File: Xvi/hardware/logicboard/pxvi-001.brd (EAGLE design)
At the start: 91 x 90 mm, 58 parts, among them J0 12V, J1 MKR, J7 DIN5, Q1 60V/32A/35mΩ, Q10 60V/32A/35mΩ, Q11 60V/32A/35mΩ, Q12 60V/32A/35mΩ, Q13 60V/32A/35mΩ, Q14 60V/32A/35mΩ, Q15 60V/32A/35mΩ, Q16 60V/32A/35mΩ, Q2 60V/32A/35mΩ, Q3 60V/32A/35mΩ, Q4 60V/32A/35mΩ, Q5 60V/32A/35mΩ, Q6 60V/32A/35mΩ, Q7 60V/32A/35mΩ, Q8 60V/32A/35mΩ, Q9 60V/32A/35mΩ, U1 DS18B20, X2 ADAFRUIT-PCA9685

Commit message: Guide for fan.
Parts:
- moved D13 2.00 mm to (51.5, 26.0)
- moved D16 2.00 mm to (84.5, 26.0)
- turned RN1 to 270 degrees
- turned RN2 to 270 degrees
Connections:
- net VCC: now also JP1.1
- net VIN: no longer JP1.1
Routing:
- net PWM06: track 216.4 -> 121.6 mm, vias 4 -> 3
- net GND: track 557.2 -> 468.9 mm, vias 1 -> 3
- net THS: track 197.7 -> 120.5 mm, vias 3 -> 4
- net VCC: track 210.6 -> 284.2 mm
- net PWM15: track 176.3 -> 132.5 mm
- net PWM04: track 134.9 -> 94.9 mm
- net SDA: track 163.1 -> 201.1 mm, vias 2 -> 5
- net PWM08: track 102.7 -> 139.0 mm, vias 3 -> 4
- net PWM10: track 161.6 -> 129.8 mm, vias 1 -> 5
- net PWM05: track 137.0 -> 107.9 mm, vias 3 -> 1
- net PWM03: track 129.7 -> 101.2 mm, vias 0 -> 3
- net LD07: track 87.8 -> 59.8 mm, vias 6 -> 0
- net LD10: track 75.0 -> 50.2 mm
- net VIN: track 399.4 -> 377.4 mm, vias 6 -> 2
- net PWM02: track 127.6 -> 106.5 mm
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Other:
- board text added: "DC5V"
- board text added: "Holes are design guide for 30mm fan"
- board text removed: "0"
- board text removed: "1"
- board text removed: "2"
- board text removed: "3"
- board text removed: "A"

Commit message: Xvi/LightDrive Port.
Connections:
- net GND: now also SV2.34
- net MNTR: now also SV2.33
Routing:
- net LD00: track 58.2 -> 185.1 mm, vias 3 -> 16
- net MNTR: track 0.00 -> 62.1 mm
- net PWM10: track 129.8 -> 173.8 mm, vias 5 -> 2
- net GND: track 468.9 -> 509.0 mm, vias 3 -> 5
- net PWM12: track 104.6 -> 137.9 mm, vias 5 -> 3
- net PWM01: track 97.2 -> 130.0 mm, vias 2 -> 3
- net PWM07: track 105.1 -> 137.9 mm, vias 6 -> 2
- net PWM15: track 132.5 -> 157.6 mm, vias 2 -> 1
- net PWM11: track 151.5 -> 175.0 mm
- net PWM04: track 94.9 -> 116.1 mm, vias 3 -> 1
- net PWM05: track 107.9 -> 128.8 mm, vias 1 -> 0
- net PWM00: track 109.8 -> 128.2 mm, vias 4 -> 3
- net VIN: track 377.4 -> 393.9 mm, vias 2 -> 4
- net LD01: track 77.7 -> 62.0 mm, vias 6 -> 3
- net PWM14: track 131.7 -> 146.3 mm, vias 4 -> 1
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- removed copper zone on layer 1, net GND
- removed copper zone on layer 16, net GND
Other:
- board text added: "LightDrive"
- board text added: "Pineapple Xvi 0.0.4-X"
- board text removed: "Pineapple Xvi 0.0.3-X"

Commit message: Redesign.
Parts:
- removed D0: (no value), SparkFun-DiscreteSemi:DIODE-1N4148
- removed D10, D11, D12, D13, D14, D15, D16, D2, D4, D5, D6, D7, D8, D9: 200mA/100V/1V, SparkFun-DiscreteSemi:DIODE-1N4148
- removed JG1: Grove/1, Connector:4P-2.0-90D
- removed JG2: Grove/2, Connector:4P-2.0-90D
- removed LD1: Red/Green, led:DUOLED-C-5MM
- removed R6: 220, resistor:0204/5
- removed RN1: 10k, resistor-net:RN-9
- removed SV2: LD, con-ml:ML34L
- removed SV3: Testport II, pinhead:2X07
- removed X2: ADAFRUIT-PCA9685, adafruit-pca9685:ADAFRUIT-PCA9685-FOOTPRINT
- added C1: 22u, rcl:C025-050X050
- added C10, C4: 100n, rcl:C025-024X044
- added C11: 100n, resistor:C025-024X044
- added C2: 470n, rcl:C050-024X044
- added C3: 1u, rcl:C050-024X044
- added C5: 10n, resistor:C025-024X044
- added DD1, DD10, DD11, DD12, DD13, DD14, DD15, DD16, DD2, DD3, DD4, DD5, DD6, DD7, DD8, DD9: 200mA/100V/1V, SparkFun-DiscreteSemi:DIODE-1N4148
- added F1: 1.8A, fuse:TE5
- added J2, J3: (no value), Connector:4P-2.0-90D
- added J20: (no value), SparkFun-Connectors:1X04_1.27MM
- added J5: SPI, SparkFun-Connectors:1X06_1.27MM
- added J6: LED, SparkFun-Connectors:JST-3-PTH-VERT
- added JP6: LED, pinhead:1X03
- added R1: 220, resistor:0204/5
- added R3: 1k, resistor:0204/5
- added SV1: (no value), con-ml:ML34L
- added V1: 5V, v-reg:78XXL
- added X1: ADAFRUIT-PCA9685, adafruit-pca9685:ADAFRUIT-PCA9685-FOOTPRINT
- D1, D3: value 200mA/100V/1V -> (none)
- J0: value 12V -> (none)
- JP1: value FAN -> PWRSEL; device pinhead:1X02 -> pinhead:2X03
- R4, R5: value 330 -> 1k
- RN2: value 10k -> 4.7k; device resistor-net:RN-9 -> resistor-net:RN-5
- moved J0 64.8 mm to (85.5, 64.0)
- moved C6 64.3 mm to (38.5, 5.00)
- moved RN2 63.5 mm to (30.0, 19.5), turned to 0 degrees
- moved D3 57.6 mm to (32.0, 14.0)
- moved J1 46.9 mm to (94.0, 23.0)
- moved C7 46.2 mm to (35.5, 58.5), turned to 0 degrees
- moved JP1 45.2 mm to (86.0, 56.5)
- moved R5 44.0 mm to (35.5, 61.5), turned to 0 degrees
- moved RN3 39.5 mm to (50.0, 24.5), turned to 0 degrees
- moved U$1 37.5 mm to (7.00, 37.5), turned to 90 degrees
- moved R4 35.7 mm to (25.5, 61.5), turned to 0 degrees
- moved LOGO1 35.5 mm to (50.0, 34.0), flipped to the top
- moved Q9 35.4 mm to (80.0, 50.0)
- moved OK1 32.0 mm to (27.0, 53.0)
- moved Q13 30.5 mm to (80.0, 30.0)
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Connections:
- removed net MIDIINSND: D0.C, OK1.1, R6.1
- new net MIN: OK1.7, RN2.2
- new net MISNDA: D3.C, OK1.1, R1.1
- new net N$10: X1.PWM02
- new net N$11: X1.PWM03
- new net N$12: X1.PWM04
- new net N$13: X1.PWM05
- new net N$14: X1.PWM06
- new net N$15: X1.PWM07
- new net N$16: X1.PWM08
- new net N$17: X1.PWM09
- new net N$18: X1.PWM10
- new net N$19: X1.PWM11
- new net N$20: X1.PWM12
- new net N$21: X1.PWM13
- new net N$22: X1.PWM14
- new net N$23: X1.PWM15
- new net N$8: X1.PWM00
- new net N$9: X1.PWM01
- new net NMO2RTN: RN2.5
- new net NMORTN: RN2.4
- new net NMTRTN: RN2.3
- new net V+: C1.1, C2.1, D1.C, DD1.C, DD10.C, DD11.C, DD12.C, DD13.C, DD14.C, DD15.C, DD16.C, DD2.C, DD3.C, DD4.C, DD5.C, DD6.C, DD7.C, DD8.C, DD9.C, J0.3, JP1.1, SV1.10, SV1.12, SV1.14, SV1.16, SV1.18, SV1.2, SV1.20, SV1.22, SV1.24, SV1.26, SV1.28, SV1.30, SV1.32, SV1.4, SV1.6, SV1.8, V1.IN
- new net VCC/2: JP1.5, R3.2
- new net VOUT: F1.2, JP1.4, JP1.6
- new net VOUTRAW: C3.1, C4.1, D1.A, F1.1, V1.OUT
- net AREF: now also C10.1, R3.1
- net D7GATE: no longer SV3.11
- net DTCT0: no longer SV3.8
- net DTCT1: no longer SV3.10
- net DTCT2: no longer SV3.12
- net DTCT3: no longer SV3.14
- net GND: now also C1.2, C10.2, C11.2, C2.2, C3.2, C4.2, C5.2, J2.4, J3.4, J5.6, J6.2, JP6.2, SV1.34, V1.GND, X1.LGND, X1.LOE, X1.RGND; no longer JG1.4, JG2.4, JP1.2, LD1.C, RN1.1, RN2.1, SV2.34, SV3.5, X2.GND00, X2.GND01, X2.GND02, X2.GND03, X2.GND04, X2.GND05, X2.GND06, X2.GND07, X2.GND08, X2.GND09, X2.GND10, X2.GND11, X2.GND12, X2.GND13, X2.GND14, X2.GND15, X2.LGND, X2.LOE, X2.RGND
- net GPIO0: now also J20.3; no longer SV3.2
- net GPIO1: now also J20.4; no longer SV3.4
- net LD00: now also DD1.A, SV1.1; no longer D1.A, SV2.1
- net LD01: now also DD2.A, SV1.3; no longer D2.A, SV2.3
- net LD02: now also DD3.A, SV1.5; no longer D3.A, SV2.5
- net LD03: now also DD4.A, SV1.7; no longer D4.A, SV2.7
- net LD04: now also DD5.A, SV1.9; no longer D5.A, SV2.9
- net LD05: now also DD6.A, SV1.11; no longer D6.A, SV2.11
- net LD06: now also DD7.A, SV1.13; no longer D7.A, SV2.13
- net LD07: now also DD8.A, SV1.15; no longer D8.A, SV2.15
- net LD08: now also DD9.A, SV1.17; no longer D9.A, SV2.17
- net LD09: now also DD10.A, SV1.19; no longer D10.A, SV2.19
- net LD10: now also DD11.A, SV1.21; no longer D11.A, SV2.21
- net LD11: now also DD12.A, SV1.23; no longer D12.A, SV2.23
- net LD12: now also DD13.A, SV1.25; no longer D13.A, SV2.25
- net LD13: now also DD14.A, SV1.27; no longer D14.A, SV2.27
- net LD14: now also DD15.A, SV1.29; no longer D15.A, SV2.29
- net LD15: now also DD16.A, SV1.31; no longer D16.A, SV2.31
- net LED0A: now also J6.3, JP6.3; no longer LD1.AR
- net LED1A: now also J6.1, JP6.1; no longer LD1.AX
- net MIRTN: now also D3.A; no longer D0.A
- net MISND: now also R1.2; no longer R6.2
- net MISO: now also J5.1
- net MNTR: now also RN3.5, SV1.33; no longer SV2.33
- net MOSI: now also J5.4
- net PWM00: no longer RN1.2, X2.PWM00
- net PWM01: no longer RN1.3, X2.PWM01
- net PWM02: no longer RN1.4, X2.PWM02
- net PWM03: no longer RN1.5, X2.PWM03
- net PWM04: no longer RN1.6, X2.PWM04
- net PWM05: no longer RN1.7, X2.PWM05
- net PWM06: no longer RN1.8, X2.PWM06
- net PWM07: no longer RN1.9, X2.PWM07
- net PWM08: no longer RN2.2, X2.PWM08
- net PWM09: no longer RN2.3, X2.PWM09
- net PWM10: no longer RN2.4, X2.PWM10
- net PWM11: no longer RN2.5, X2.PWM11
- net PWM12: no longer RN2.6, X2.PWM12
- net PWM13: no longer RN2.7, X2.PWM13
- net PWM14: no longer RN2.8, X2.PWM14
- net PWM15: no longer RN2.9, X2.PWM15
- net RST: now also J5.5
- net RX: no longer OK1.7, RN3.5, SV3.3
- net SCK: now also J5.3
- net SCL: now also J2.1, J3.1, X1.LSCL; no longer JG1.1, JG2.1, SV3.9, X2.LSCL
- net SDA: now also J2.2, J3.2, X1.LSDA; no longer JG1.2, JG2.2, SV3.7, X2.LSDA
- net THS: no longer SV3.6
- net TX: no longer SV3.1
- net VCC: now also C11.1, C5.1, J2.3, J3.3, J5.2, JP1.3, RN2.1, X1.LVCC; no longer JG1.3, JG2.3, JP1.1, SV3.13, X2.LVCC
- net VIN: now also JP1.2; no longer D1.C, D10.C, D11.C, D12.C, D13.C, D14.C, D15.C, D16.C, D2.C, D3.C, D4.C, D5.C, D6.C, D7.C, D8.C, D9.C, J0.3, SV2.10, SV2.12, SV2.14, SV2.16, SV2.18, SV2.2, SV2.20, SV2.22, SV2.24, SV2.26, SV2.28, SV2.30, SV2.32, SV2.4, SV2.6, SV2.8, X2.LV+, X2.RV+, X2.V+00, X2.V+01, X2.V+02, X2.V+03, X2.V+04, X2.V+05, X2.V+06, X2.V+07, X2.V+08, X2.V+09, X2.V+10, X2.V+11, X2.V+12, X2.V+13, X2.V+14, X2.V+15
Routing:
- net GND: track 509.0 -> 0.00 mm, vias 5 -> 0
- net VIN: track 393.9 -> 0.00 mm, vias 4 -> 0
- net VCC: track 278.9 -> 0.00 mm, vias 8 -> 0
- net SDA: track 199.2 -> 0.00 mm, vias 3 -> 0
- net LD00: track 185.1 -> 0.00 mm, vias 16 -> 0
- net PWM11: track 175.0 -> 0.00 mm, vias 1 -> 0
- net PWM10: track 173.8 -> 0.00 mm, vias 2 -> 0
- net SCL: track 172.5 -> 0.00 mm, vias 3 -> 0
- net PWM15: track 157.6 -> 0.00 mm, vias 1 -> 0
- net PWM14: track 146.3 -> 0.00 mm, vias 1 -> 0
- net PWM12: track 137.9 -> 0.00 mm, vias 3 -> 0
- net PWM07: track 137.9 -> 0.00 mm, vias 2 -> 0
- net PWM06: track 134.1 -> 0.00 mm, vias 1 -> 0
- net PWM08: track 130.8 -> 0.00 mm, vias 6 -> 0
- net PWM01: track 130.0 -> 0.00 mm, vias 3 -> 0
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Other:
- board size 91 x 90 mm -> 100 x 75 mm
- board text added: "0"
- board text added: "00"
- board text added: "01"
- board text added: "02"
- board text added: "03"
- board text added: "1"
- board text added: "102"
- board text added: "2"
- board text added: "2630"
- board text added: "Arduino Only"
- board text added: "C1: 22u C2: 470n C3: 1u C4: 100n C5-8: 10n C9-10: 100n"
- board text added: "Designed for Takachi PF13-4-9"
- board text added: "Direct 5V"
- board text added: "Do not install R301 or R302"
- board text added: "Dual Regulator"
- board text added: "I"
- board text added: "IN"
- board text added: "LED"
- board text added: "LED00"
- board text added: "M"
- board text added: "MN"
- board text added: "O"
- board text added: "SC"
- board text added: "SD"
- board text added: "Single Regulator"
- board text added: "T"
- board text added: "T*"
- board text added: "THS*"
- board text added: "TestPort II"
- board text added: "USB"
- board text added: "V"
- board text added: "Vcc/2"
- board text added: "Vout"
- board text removed: "*"
- board text removed: "104"
- board text removed: "2-103"
- board text removed: "331"
- board text removed: "DC5V"
- board text removed: "Designed for Takachi PF10-4-10"
- board text removed: "Grove"
- board text removed: "Holes are design guide for 30mm fan"
- board text removed: "K"
- board text removed: "LightDrive"
- board text removed: "MIDI"
- board text removed: "R"
- board text removed: "TLP2630"
- board text removed: "Test Port II"
- board text removed: "Vdd"
- board text removed: "X0"
- board text removed: "X1"
- board text removed: "X2"
- board text removed: "X3"

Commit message: Arrangement.
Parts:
- removed J6: LED, SparkFun-Connectors:JST-3-PTH-VERT
- DD1, DD10, DD11, DD12, DD13, DD14, DD15, DD16, DD2, DD3, DD4, DD5, DD6, DD7, DD8, DD9: value 200mA/100V/1V -> 250mA/100V; device SparkFun-DiscreteSemi:DIODE-1N4148 -> SparkFun-DiscreteSemi:SOD-323
- moved DD10 223.6 mm to (87.0, 45.0), turned to 90 degrees
- moved DD11 223.6 mm to (87.0, 40.0), turned to 90 degrees
- moved DD12 223.6 mm to (87.0, 35.0), turned to 90 degrees
- moved DD13 223.6 mm to (87.0, 30.0), turned to 90 degrees
- moved DD14 223.6 mm to (87.0, 25.0), turned to 90 degrees
- moved DD15 223.6 mm to (87.0, 20.0), turned to 90 degrees
- moved DD16 223.6 mm to (87.0, 15.0), turned to 90 degrees
- moved DD9 223.6 mm to (87.0, 50.0), turned to 90 degrees
- moved DD1 180.9 mm to (72.0, 50.0), turned to 90 degrees
- moved DD2 180.9 mm to (72.0, 45.0), turned to 90 degrees
- moved DD3 180.9 mm to (72.0, 40.0), turned to 90 degrees
- moved DD4 180.9 mm to (72.0, 35.0), turned to 90 degrees
- moved DD5 180.9 mm to (72.0, 30.0), turned to 90 degrees
- moved DD6 180.9 mm to (72.0, 25.0), turned to 90 degrees
- moved DD7 180.9 mm to (72.0, 20.0), turned to 90 degrees
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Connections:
- net GND: no longer J6.2
- net LED0A: no longer J6.3
- net LED1A: no longer J6.1
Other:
- board text removed: "00"
- board text removed: "01"
- board text removed: "02"
- board text removed: "03"
- board text removed: "102"
- board text removed: "103"
- board text removed: "2630"
- board text removed: "G"
- board text removed: "G0"
- board text removed: "G1"
- board text removed: "IN"
- board text removed: "LED00"
- board text removed: "RX"
- board text removed: "TH"
- board text removed: "TX"
- board text removed: "TestPort II"
- board text removed: "V"
- board text removed: "V+"
- board text removed: "Vcc/2"
- board text removed: "Vin"
- board text removed: "Vout"

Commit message: Routed.
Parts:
- removed C10: 100n, rcl:C025-024X044
- removed C11, C9: 100n, resistor:C025-024X044
- removed C8: 10n, resistor:C025-024X044
- removed F1: 1.8A, fuse:TE5
- removed JP1: PWRSEL, pinhead:2X03
- removed R3: 1k, resistor:0204/5
- removed RN2: 4.7k, resistor-net:RN-5
- moved U1 85.4 mm to (10.0, 71.0)
- moved J1 71.1 mm to (25.0, 6.00), turned to 180 degrees
- moved C3 70.8 mm to (94.0, 49.0)
- moved C4 70.8 mm to (94.0, 52.0)
- moved R4 68.7 mm to (94.0, 56.0)
- moved C6 66.1 mm to (35.0, 71.0), turned to 180 degrees
- moved C2 65.0 mm to (90.0, 20.0), turned to 90 degrees
- moved C1 59.6 mm to (95.0, 20.0)
- moved D1 58.6 mm to (94.0, 25.0)
- moved C7 54.5 mm to (35.0, 4.00)
- moved RN3 52.8 mm to (25.0, 71.0)
- moved R5 50.8 mm to (86.0, 56.0)
- moved OK1 40.2 mm to (50.0, 20.0)
- moved R1 26.2 mm to (43.0, 20.0), turned to 90 degrees
- moved D3 25.7 mm to (57.0, 20.0), turned to 90 degrees
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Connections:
- removed net MIN: OK1.7, RN2.2
- removed net N$10: X1.PWM02
- removed net N$11: X1.PWM03
- removed net N$12: X1.PWM04
- removed net N$13: X1.PWM05
- removed net N$14: X1.PWM06
- removed net N$15: X1.PWM07
- removed net N$16: X1.PWM08
- removed net N$17: X1.PWM09
- removed net N$18: X1.PWM10
- removed net N$19: X1.PWM11
- removed net N$20: X1.PWM12
- removed net N$21: X1.PWM13
- removed net N$22: X1.PWM14
- removed net N$23: X1.PWM15
- removed net N$8: X1.PWM00
- removed net N$9: X1.PWM01
- removed net NMO2RTN: RN2.5
- removed net NMORTN: RN2.4
- removed net NMTRTN: RN2.3
- removed net VCC/2: JP1.5, R3.2
- removed net VOUT: F1.2, JP1.4, JP1.6
- removed net VOUTRAW: C3.1, C4.1, D1.A, F1.1, V1.OUT
- net AREF: no longer C10.1, R3.1
- net GND: no longer C10.2, C11.2, C8.2, C9.2
- net MNTR: no longer RN3.5
- net PWM00: now also X1.PWM00
- net PWM01: now also X1.PWM01
- net PWM02: now also X1.PWM02
- net PWM03: now also X1.PWM03
- net PWM04: now also X1.PWM04
- net PWM05: now also X1.PWM05
- net PWM06: now also X1.PWM06
- net PWM07: now also X1.PWM07
- net PWM08: now also X1.PWM08
- net PWM09: now also X1.PWM09
- net PWM10: now also X1.PWM10
- net PWM11: now also X1.PWM11
- net PWM12: now also X1.PWM12
- net PWM13: now also X1.PWM13
- net PWM14: now also X1.PWM14
- net PWM15: now also X1.PWM15
- net RX: now also OK1.7, RN3.5
- net V+: no longer JP1.1
- net VCC: now also C3.1, C4.1, D1.A, V1.OUT; no longer C11.1, C8.1, C9.1, JP1.3, RN2.1
- net VIN: no longer JP1.2
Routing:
- net GND: track 0.00 -> 427.9 mm, vias 0 -> 1
- net VCC: track 0.00 -> 252.2 mm, vias 0 -> 2
- net V+: track 0.00 -> 182.0 mm, vias 0 -> 4
- net SCL: track 0.00 -> 140.8 mm, vias 0 -> 1
- net SDA: track 0.00 -> 138.8 mm, vias 0 -> 4
- net D7GATE: track 0.00 -> 96.0 mm, vias 0 -> 1
- net PWM09: track 0.00 -> 94.9 mm, vias 0 -> 2
- net PWM08: track 0.00 -> 89.1 mm, vias 0 -> 2
- net PWM12: track 0.00 -> 83.5 mm
- net LD08: track 0.00 -> 83.4 mm, vias 0 -> 2
- net PWM14: track 0.00 -> 76.5 mm
- net LD00: track 0.00 -> 72.4 mm
- net PWM13: track 0.00 -> 72.2 mm, vias 0 -> 1
- net PWM15: track 0.00 -> 72.1 mm
- net MOSI: track 0.00 -> 70.3 mm, vias 0 -> 1
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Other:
- board text removed: "2"
- board text removed: "472"
- board text removed: "D7"
- board text removed: "GND"
- board text removed: "I"
- board text removed: "M"
- board text removed: "MN"
- board text removed: "O"
- board text removed: "SC"
- board text removed: "SCL"
- board text removed: "SD"
- board text removed: "SDA"
- board text removed: "T"
- board text removed: "T*"
- board text removed: "Vcc"

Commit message: Routed.
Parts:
- added X2: MKDSN1,5/2-5,08, con-phoenix-508:MKDSN1,5/2-5,08
- DD1, DD10, DD11, DD12, DD13, DD14, DD15, DD16, DD2, DD3, DD4, DD5, DD6, DD7, DD8, DD9: value 250mA/100V -> CGRM400-G; device SparkFun-DiscreteSemi:SOD-323 -> diode:SOD-123_MINI-SMA
- moved LOGO1 41.6 mm to (8.50, 37.5), turned to 90 degrees
- moved DD2 1.12 mm to (72.5, 46.0), flipped to the bottom
- moved DD4 1.12 mm to (72.5, 36.0), flipped to the bottom
- moved DD6 1.12 mm to (72.5, 26.0), flipped to the bottom
- moved DD8 1.12 mm to (72.5, 16.0), flipped to the bottom
- moved DD10 1.00 mm to (87.0, 46.0), flipped to the bottom
- moved DD12 1.00 mm to (87.0, 36.0), flipped to the bottom
- moved DD14 1.00 mm to (87.0, 26.0), flipped to the bottom
- moved DD16 1.00 mm to (87.0, 16.0), flipped to the bottom
- moved U$1 1.00 mm to (6.00, 37.5)
- moved DD1 0.71 mm to (72.5, 50.5)
- moved DD3 0.71 mm to (72.5, 40.5)
- moved DD5 0.71 mm to (72.5, 30.5)
- moved DD7 0.71 mm to (72.5, 20.5)
- moved DD11 0.50 mm to (87.0, 40.5)
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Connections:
- net GND: now also X2.2
- net VCC: now also X2.1
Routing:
- net GND: track 427.9 -> 483.9 mm
- net LD09: track 48.7 -> 82.6 mm, vias 1 -> 2
- net VCC: track 252.2 -> 282.2 mm, vias 2 -> 1
- net LD14: track 38.0 -> 65.9 mm, vias 0 -> 1
- net D7GATE: track 96.0 -> 69.0 mm, vias 1 -> 2
- net PWM06: track 56.0 -> 82.2 mm, vias 2 -> 0
- net PWM09: track 94.9 -> 68.6 mm, vias 2 -> 1
- net PWM12: track 83.5 -> 66.0 mm, vias 0 -> 1
- net SCL: track 140.8 -> 158.4 mm
- net PWM08: track 89.1 -> 73.4 mm
- net V+: track 182.0 -> 196.2 mm, vias 4 -> 8
- net LD08: track 83.4 -> 69.8 mm, vias 2 -> 6
- net PWM07: track 60.1 -> 73.0 mm, vias 2 -> 0
- net PWM04: track 64.2 -> 52.2 mm
- net GPIO0: track 69.8 -> 81.7 mm, vias 1 -> 0
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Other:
- board text removed: "Arduino Only"
- board text removed: "Direct 5V"
- board text removed: "Dual Regulator"
- board text removed: "Single Regulator"

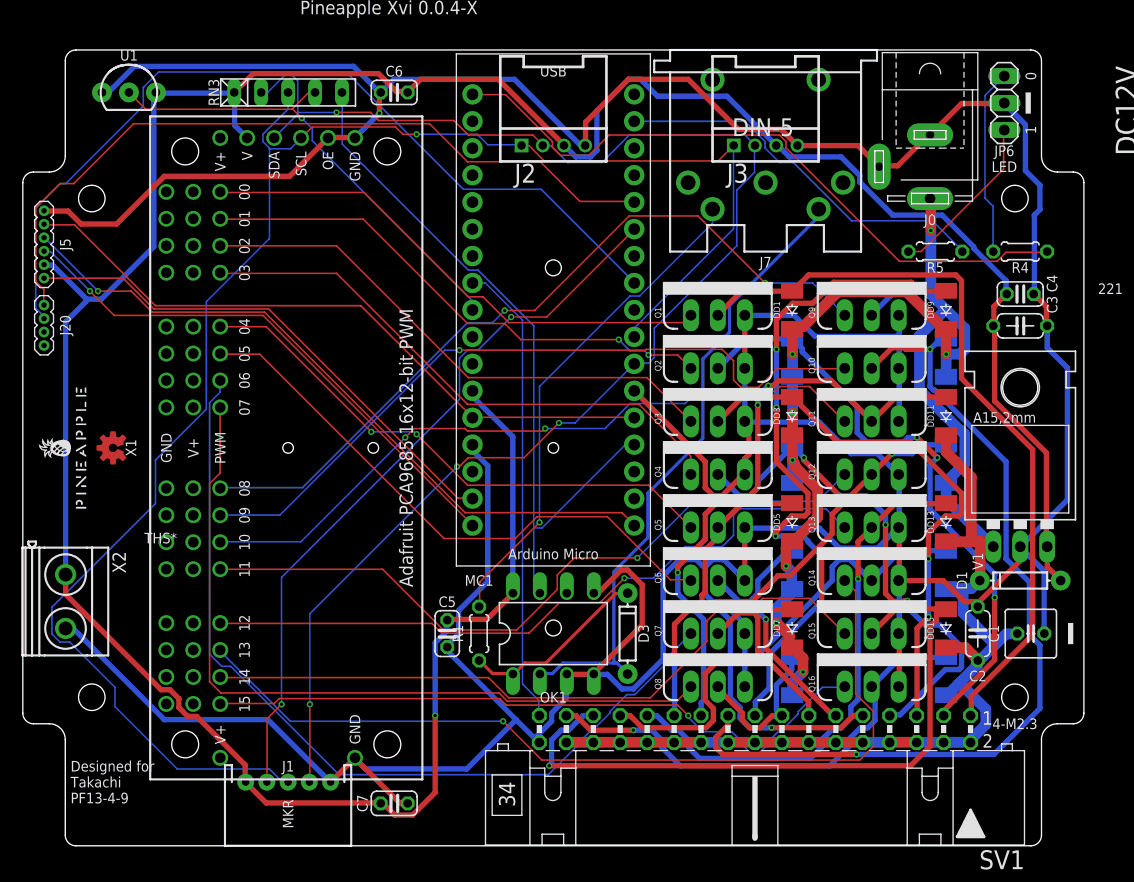
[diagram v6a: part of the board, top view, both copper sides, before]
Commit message: Diodes -> back.
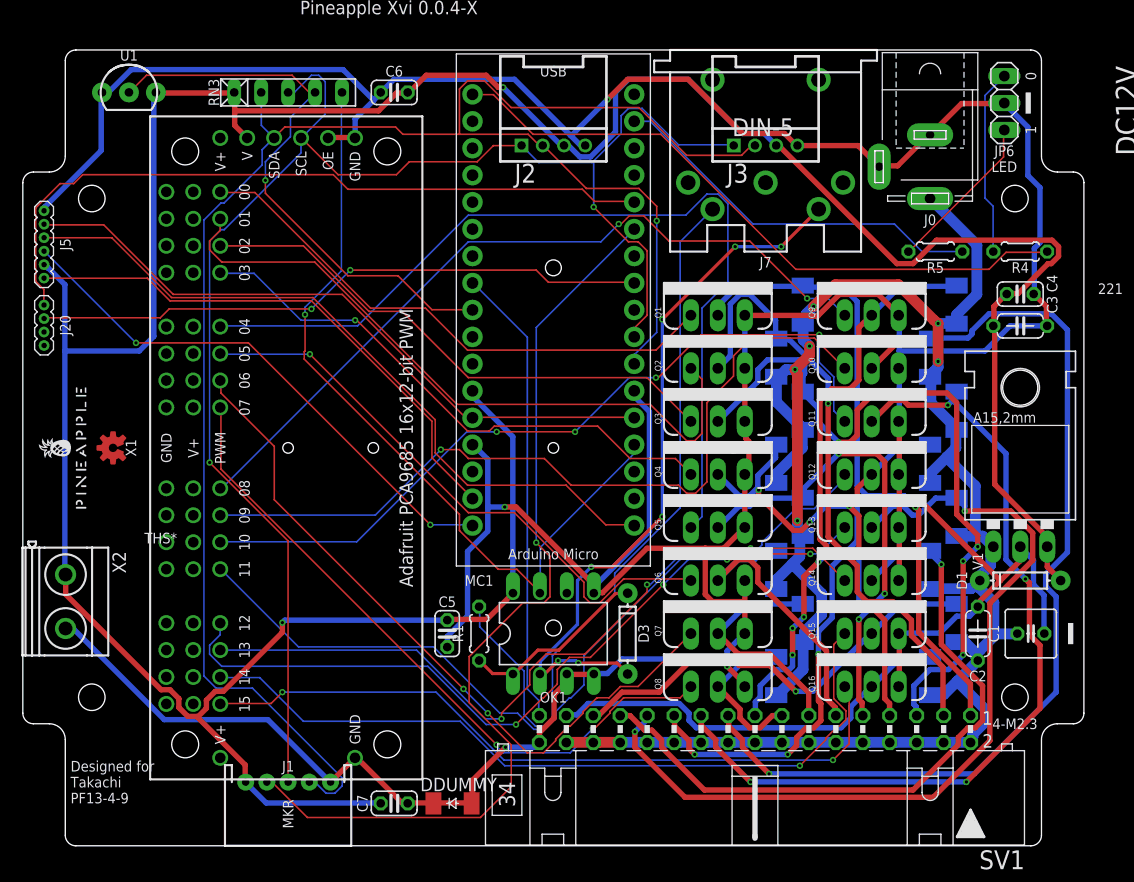
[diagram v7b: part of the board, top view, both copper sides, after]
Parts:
- added DDUMMY: CGRM400-G, diode:SOD-123_MINI-SMA
- moved DD10 1.50 mm to (85.5, 46.0)
- moved DD12 1.50 mm to (85.5, 36.0)
- moved DD14 1.50 mm to (85.5, 26.0)
- moved DD16 1.50 mm to (85.5, 16.0)
- moved DD2 1.50 mm to (71.0, 46.0)
- moved DD4 1.50 mm to (71.0, 36.0)
- moved DD6 1.50 mm to (71.0, 26.0)
- moved DD8 1.50 mm to (71.0, 16.0)
- moved DD1 1.12 mm to (73.5, 51.0), flipped to the bottom
- moved DD11 1.12 mm to (88.0, 41.0), flipped to the bottom
- moved DD13 1.12 mm to (88.0, 31.0), flipped to the bottom
- moved DD15 1.12 mm to (88.0, 21.0), flipped to the bottom
- moved DD3 1.12 mm to (73.5, 41.0), flipped to the bottom
- moved DD5 1.12 mm to (73.5, 31.0), flipped to the bottom
- moved DD7 1.12 mm to (73.5, 21.0), flipped to the bottom
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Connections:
- net GND: now also DDUMMY.A, DDUMMY.C
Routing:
- net GND: track 483.9 -> 436.8 mm, vias 1 -> 4
- net PWM04: track 52.2 -> 85.4 mm, vias 2 -> 0
- net SDA: track 139.5 -> 171.1 mm, vias 4 -> 1
- net LD12: track 50.0 -> 81.0 mm, vias 1 -> 2
- net LD14: track 65.9 -> 41.2 mm
- net LD10: track 56.6 -> 80.6 mm, vias 3 -> 4
- net GPIO0: track 81.7 -> 58.0 mm, vias 0 -> 2
- net VCC: track 282.2 -> 304.9 mm, vias 1 -> 2
- net MISND: track 47.1 -> 69.5 mm, vias 1 -> 0
- net LD13: track 44.2 -> 65.3 mm
- net D7GATE: track 69.0 -> 88.5 mm, vias 2 -> 1
- net LD02: track 51.1 -> 68.9 mm, vias 2 -> 4
- net LD08: track 69.8 -> 53.7 mm, vias 6 -> 5
- net PWM06: track 82.2 -> 67.3 mm, vias 0 -> 2
- net PWM01: track 50.2 -> 64.1 mm, vias 2 -> 0
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
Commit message: Relay.
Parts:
- added C8: 10n, resistor:C025-024X044
- added K1: G5V1, relay:G5V1
- added R2, R3: 1k, resistor:0204/5
- added T1: 2SC1815, transistor:TO92-ECB
- moved LOGO1 34.1 mm to (15.0, 4.00), turned to 0 degrees
- moved X2 14.5 mm to (4.50, 37.5)
- moved U$1 9.00 mm to (-3.00, 37.5)
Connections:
- new net N$1: K1.9, T1.C
- new net N$2: R2.2, R3.2, T1.B
- new net N$4: K1.10, X2.2
- net GND: now also C8.2, R3.1, T1.E, X2.1; no longer X2.2
- net RLY: now also R2.1
- net VCC: now also C8.1, K1.2, K1.5, K1.6; no longer X2.1
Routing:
- net RLY: track 0.00 -> 65.5 mm
- net MIRTN: track 67.7 -> 124.7 mm, vias 7 -> 1
- net V+: track 192.3 -> 245.2 mm, vias 6 -> 11
- net LD09: track 94.2 -> 46.5 mm, vias 2 -> 1
- net GND: track 436.8 -> 480.2 mm, vias 4 -> 5
- net LD00: track 60.9 -> 90.2 mm, vias 1 -> 2
- net LD12: track 81.0 -> 53.1 mm, vias 2 -> 7
- net N$1: track 0.00 -> 26.9 mm
- net PWM12: track 74.4 -> 99.7 mm, vias 4 -> 3
- net LD01: track 58.1 -> 82.9 mm, vias 1 -> 10
- net SDA: track 171.1 -> 148.4 mm, vias 1 -> 3
- net LD11: track 50.2 -> 72.1 mm, vias 4 -> 3
- net LD02: track 68.9 -> 48.1 mm, vias 4 -> 3
- net LD05: track 28.6 -> 48.8 mm, vias 0 -> 3
- net GPIO0: track 58.0 -> 78.2 mm, vias 2 -> 1
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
